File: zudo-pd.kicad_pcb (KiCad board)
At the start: 2 copper layers, 82 x 99 mm, 92 parts, among them J1 USB-C, J10 2541WR-2X08P, J11 2541WR-2X08P, J2 Pogo pads, J3 Pogo pads (debug), J6 1217754-1, J7 1217754-1, J8 1217754-1, J9 1217754-1, Q1 -30V -4A, U1 STUSB4500QTR, U2 LM2596S-ADJ, U3 LM2596S-ADJ, U4 LM2596S-ADJ, U6 L7812CD2T-TR, U7 L7805ABD2T-TR, U8 CJ7912_C94173

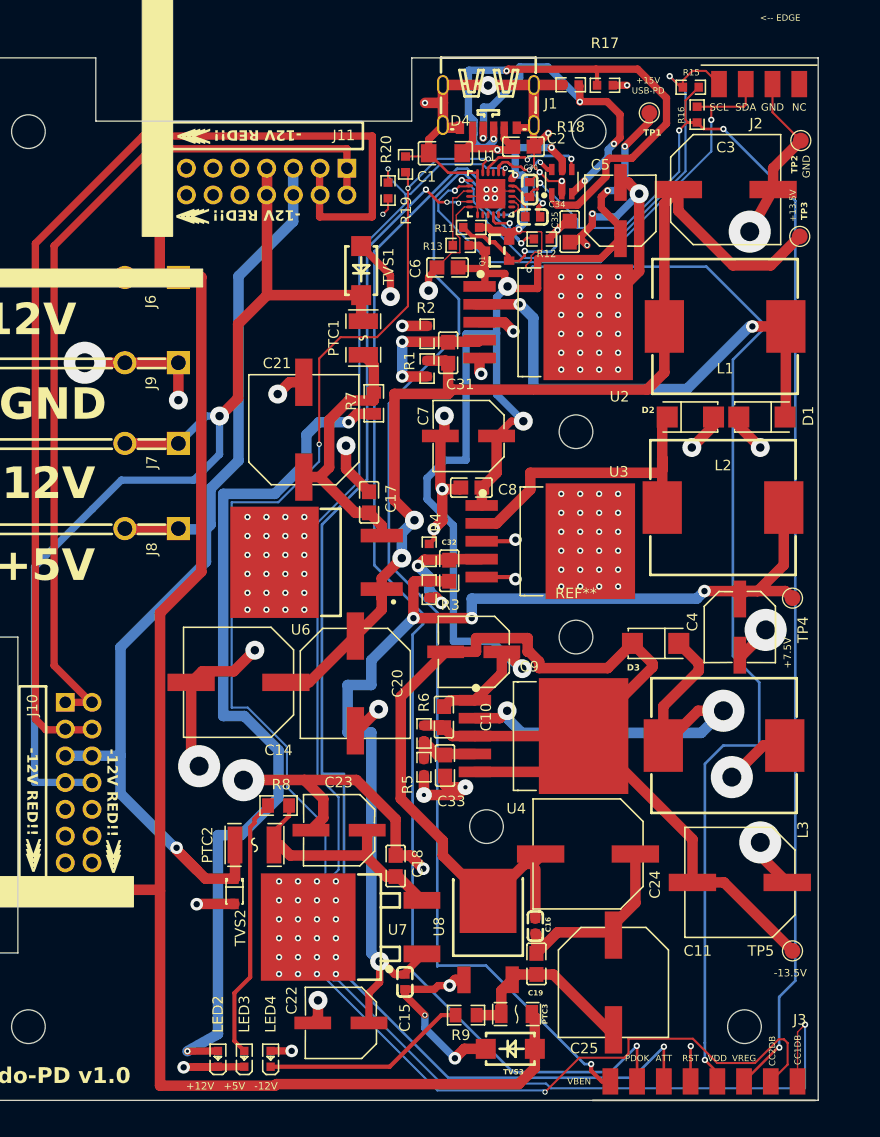
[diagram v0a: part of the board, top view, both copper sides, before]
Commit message: fix(usb-pd): wire STUSB4500 pin18 VBUS_VS_DISCH to VBUS_IN via R14 series resistor
This fixes the root cause of v3 failing to negotiate USB-PD. Pin 18
(VBUS_VS_DISCH) was left floating. Corrections:
- Wire pin 18 to VBUS_IN through series resistor R14 (470Ω)
- Add test point TP6 on VBUS_VS_DISCH net for diagnostics
- Fix R14 footprint from unresolved easyeda2kicad:R0603 to zudo-pd:R0603
- Remove incorrect divider-to-GND resistor network (now single series topology)
- Update PCB layout to match schematic changes (R14 placement, TP6, routing)

Co-Authored-By: Claude Opus 4.8 (1M context) <noreply@anthropic.com>
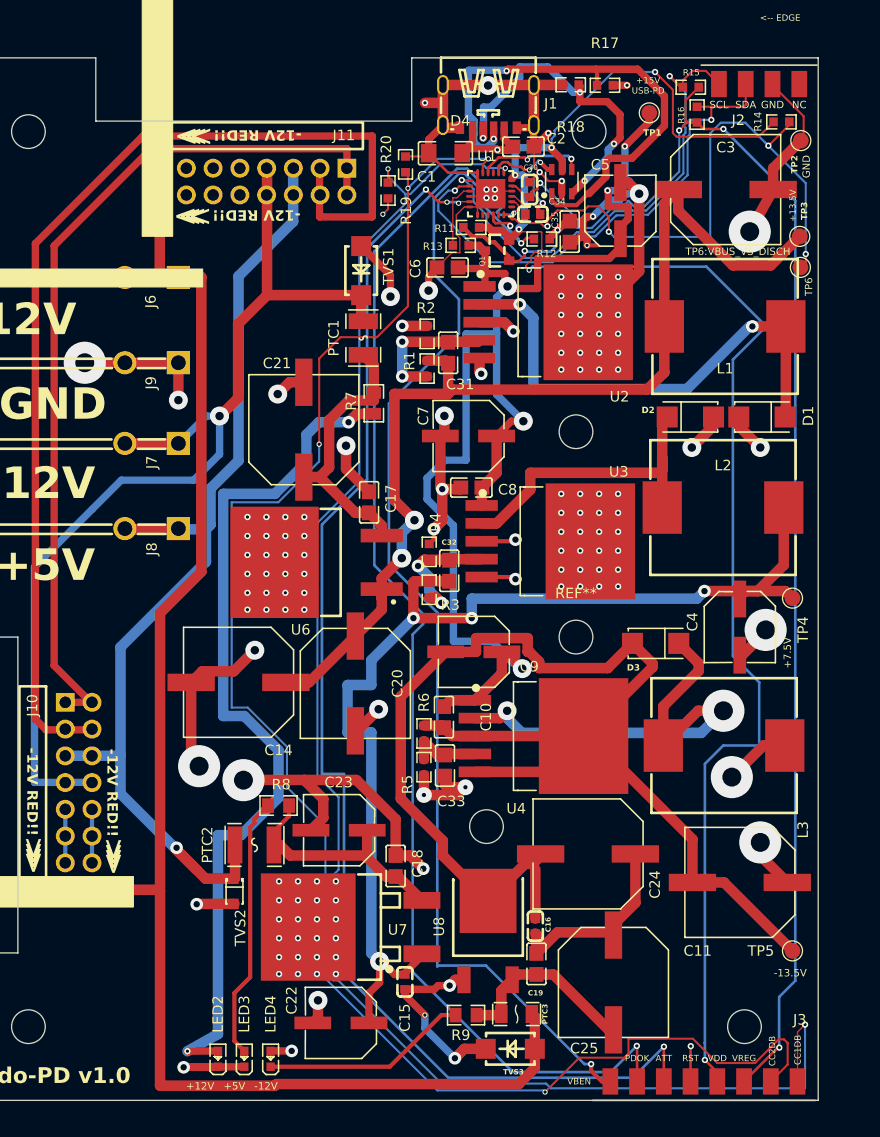
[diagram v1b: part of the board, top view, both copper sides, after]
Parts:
- added R14: 470ohm, zudo-pd:R0603, F.Cu at (72.5, 6.08)
- added TP6: VBUS_VS_DISCH, TestPoint:TestPoint_Pad_D1.5mm, F.Cu at (74.3, 19.9)
- moved C34 0.26 mm to (48.9, 14.8)
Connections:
- U1 pad 18: unconnected-(R14-Pad1) -> VBUS_VS_DISCH
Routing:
- net VBUS_VS_DISCH: track 0.00 -> 56.2 mm, vias 0 -> 4
- net VBUS_IN: track 143.3 -> 174.2 mm, vias 6 -> 7
- net GND rail: track 298.7 -> 319.5 mm
- net VBUS_OUT: track 119.3 -> 121.0 mm
- net SDA-pin2: track 48.0 -> 49.4 mm
- net Net-(J1-CC2): track 32.1 -> 31.5 mm
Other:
- board text added: "TP6:VBUS_VS_DISCH"

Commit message: fix(usb-pd): v0.4.0 faston swap to C591344 + harmonize BOM comments
- J6-J9 faston: C305825 (TE 1217754-1, out of stock) -> C591344
  (TE 63951-1, same physical tab/footprint, strip packaging)
- Harmonize Comment/Value so duplicate-LCSC lines collapse to one
  BOM row each: 470ohm (R13,R14), 100nF 50V (8x), 470uF 16V (C4,C22,C23)
- PCB synced from schematic (Update PCB from Schematic)

Co-Authored-By: Claude Opus 4.8 (1M context) <noreply@anthropic.com>
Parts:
- C10, C17, C18, C19, C2, C6, C8: value 100nF -> 100nF 50V
- C22, C23: value 470uF -> 470uF 16V
- J6, J7, J8, J9: value 1217754-1 -> 63951-1
- R13: value 470 -> 470ohm
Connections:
- net GND rail renamed GND
- net VBUS_OUT renamed +15V -> +13.5V gen
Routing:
- added copper zone on B.Cu, net (none)
- removed copper zone on B.Cu, net GND
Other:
- board text added: "zudo-PD v0.4.0"
- board text removed: "zudo-PD v1.0"
